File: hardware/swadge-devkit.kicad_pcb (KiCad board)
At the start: 2 copper layers, 100 x 100 mm, 60 parts, among them J1 USB_B_Micro, SW1 SW_SPDT, SW2 4-1437565-2, SW3 4-1437565-2, SW4 4-1437565-2, SW5 4-1437565-2, U1 ESP-12F, U2 MCP6001-OT, U3 MSA300, U4 AP1117-33, U5 BUS_PCIexpress, U6 DISP_OLED_UG-2864HSWEG01, U7 2460, U8 2460, U9 MMA8452Q

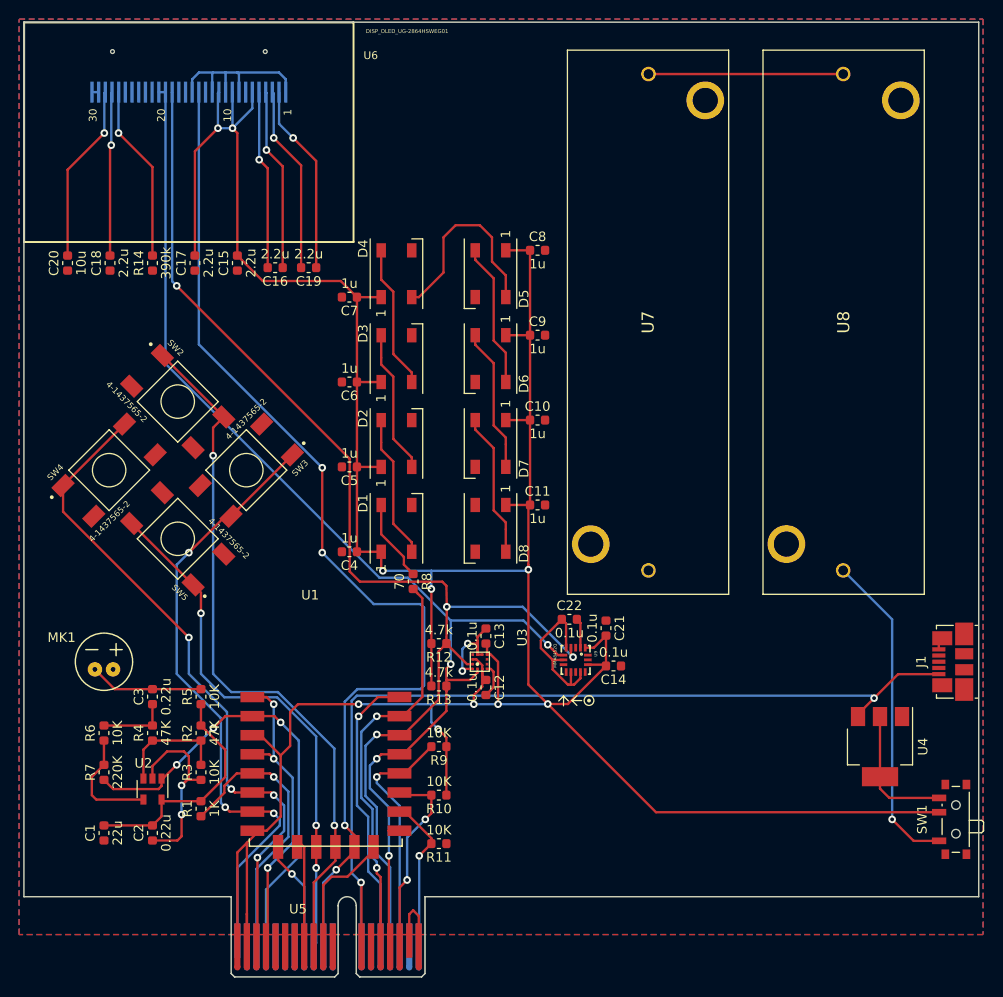
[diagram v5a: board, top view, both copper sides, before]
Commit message: Made board symmetrical wrt. the PCI connector
Moved batteries to the back, imported Swadge 2019 battery footprint
Reoriented accelerometers so they match orientation
Fattened up power traces
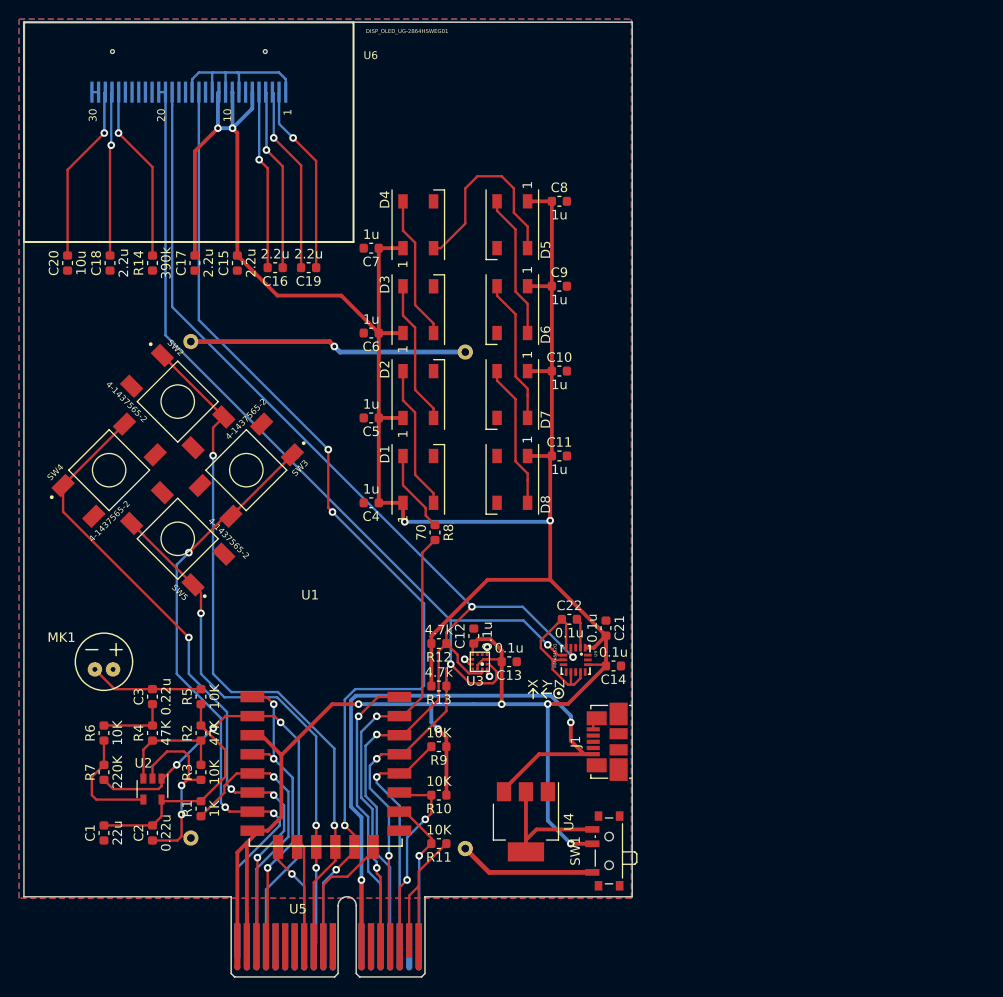
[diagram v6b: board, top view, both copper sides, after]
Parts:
- removed U7, U8: 2460, Swadge_Parts:2460
- added BT1: Battery, Swadge_Parts:BCAAPC, B.Cu at (131.0, 107.3)
- added BT2: Battery, Swadge_Parts:BCAAPC, B.Cu at (159.8, 107.3)
- moved U4 37.9 mm to (166.1, 131.1)
- moved J1 37.2 mm to (174.6, 122.7)
- moved SW1 36.5 mm to (174.5, 134.1)
- moved C10 5.62 mm to (169.6, 83.9)
- moved C11 5.62 mm to (169.6, 92.7)
- moved C4 5.62 mm to (149.9, 97.7)
- moved C5 5.62 mm to (149.9, 88.8)
- moved C6 5.62 mm to (149.9, 79.9)
- moved C7 5.62 mm to (149.9, 71.0)
- moved C8 5.62 mm to (169.6, 66.1)
- moved C9 5.62 mm to (169.6, 75.0)
- moved D1 5.62 mm to (154.8, 95.2)
- moved D2 5.62 mm to (154.8, 86.3)
- moved D3 5.62 mm to (154.8, 77.4)
- moved D4 5.62 mm to (154.8, 68.5)
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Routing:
- net Net-(BT1-Pad1): track 0.00 -> 29.2 mm, vias 0 -> 1
- net +5V: track 98.1 -> 73.8 mm
- net Net-(U7-Pad1): track 20.4 -> 0.00 mm
- net Net-(BT2-Pad1): track 34.1 -> 14.3 mm, vias 1 -> 0
- net +3V3: track 338.1 -> 319.4 mm, vias 10 -> 9
- net RX: track 42.8 -> 48.1 mm
- net SCL: track 132.8 -> 129.6 mm, vias 4 -> 3
- net MOSI: track 109.9 -> 107.2 mm
- net SDA: track 127.9 -> 130.2 mm
- net GND: track 80.0 -> 80.4 mm, vias 4 -> 5
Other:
- board size 100 x 100 mm -> 63.7 x 100 mm

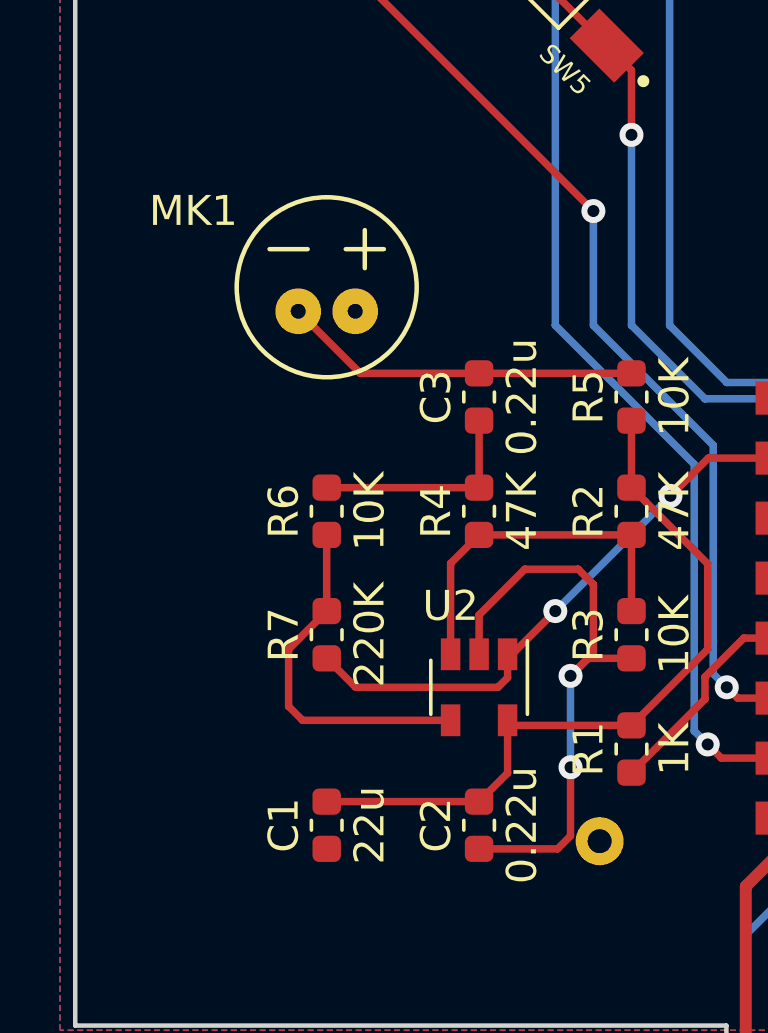
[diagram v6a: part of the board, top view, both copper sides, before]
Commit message: Moved mic away from battery
Updated DRC to use CNLohr's numbers
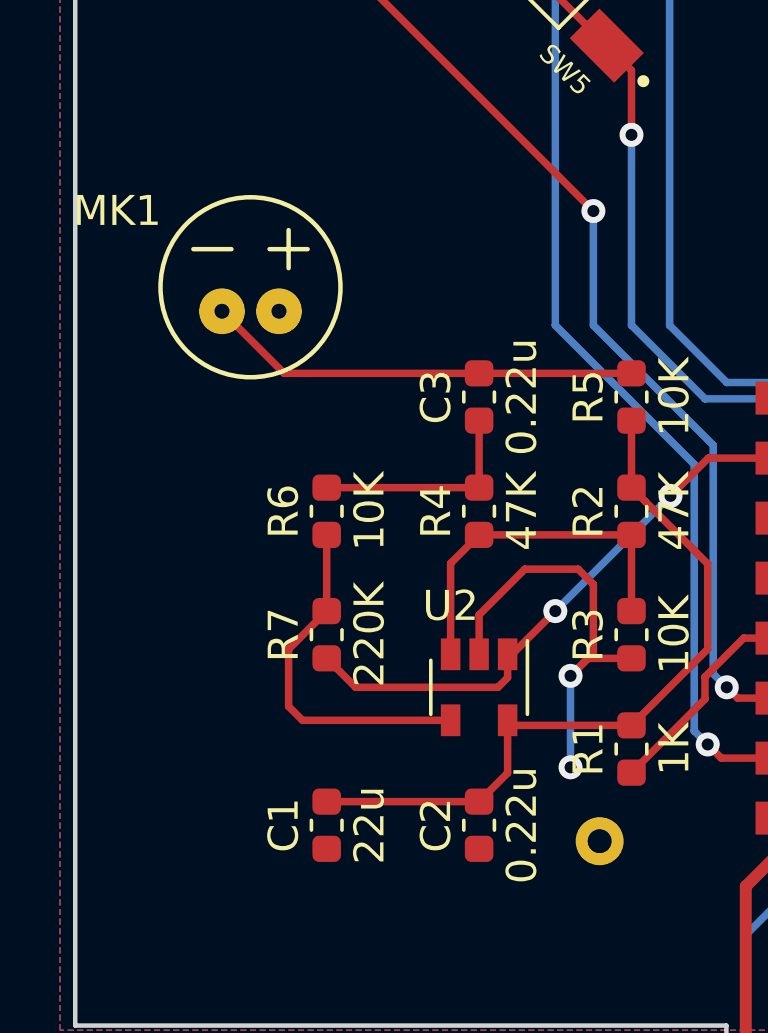
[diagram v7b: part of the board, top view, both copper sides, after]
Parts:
- moved MK1 2.54 mm to (119.4, 114.3)
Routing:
- net GND: track 80.4 -> 74.9 mm
- net Net-(C3-Pad2): track 12.0 -> 14.5 mm
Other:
- net class Default: clearance 0.2 -> 0.19558; trace_width 0.25 -> 0.3048; via_dia 0.8 -> 0.635; via_drill 0.4 -> 0.3556
- rule trace_clearance: 0.2 -> 0.19558
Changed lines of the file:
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@@
-(kicad_pcb (version 20171130) (host pcbnew "(5.0.0)")
+(kicad_pcb (version 20171130) (host pcbnew "(5.0.2)-1")
   (general
     (thickness 1.6)
     (drawings 25)
-    (tracks 579)
+    (tracks 576)
     (zones 0)
     (modules 60)
@@
   )
   (setup
-    (last_trace_width 0.4)
+    (last_trace_width 0.3048)
     (user_trace_width 0.4)
-    (trace_clearance 0.2)
+    (trace_clearance 0.19558)
     (zone_clearance 0.05)
     (zone_45_only no)
@@
     (segment_width 0.01)
     (edge_width 0.15)
-    (via_size 0.8)
-    (via_drill 0.4)
+    (via_size 0.635)
+    (via_drill 0.3556)
     (via_min_size 0.4)
     (via_min_drill 0.3)
@@
   (net 75 "Net-(BT2-Pad1)")
   (net_class Default "This is the default net class."
-    (clearance 0.2)
-    (trace_width 0.25)
-    (via_dia 0.8)
-    (via_drill 0.4)
+    (clearance 0.19558)
+    (trace_width 0.3048)
+    (via_dia 0.635)
+    (via_drill 0.3556)
     (uvia_dia 0.3)
     (uvia_drill 0.1)
@@
   )
   (module Swadge_Parts:POM-2738P-R (layer F.Cu)
-    (at 121.92 114.3 180)
+    (at 119.38 114.3 180)
     (fp_text reference MK1 (at 4.445 2.54 180) (layer F.SilkS)
       (effects (font (size 1 1) (thickness 0.15)))
@@
   (via (at 130.048 130.302) (size 0.8) (drill 0.4) (layers F.Cu B.Cu) (net 3))
   (segment (start 130.048 127.254) (end 130.048 130.302) (width 0.25) (layer B.Cu) (net 3))
-  (segment (start 130.048 130.302) (end 130.048 132.588) (width 0.25) (layer F.Cu) (net 3))
-  (segment (start 129.616 133.02) (end 127 133.02) (width 0.25) (layer F.Cu) (net 3))
-  (segment (start 130.048 132.588) (end 129.616 133.02) (width 0.25) (layer F.Cu) (net 3))
   (segment (start 127 126.535) (end 127 125.222) (width 0.25) (layer F.Cu) (net 3))
   (segment (start 127 125.222) (end 128.524 123.698) (width 0.25) (layer F.Cu) (net 3))
@@
   (segment (start 127 120.98) (end 121.92 120.98) (width 0.25) (layer F.Cu) (net 4))
   (segment (start 127 117.17) (end 132.08 117.17) (width 0.25) (layer F.Cu) (net 5))
-  (segment (start 123.04 117.17) (end 120.97 115.1) (width 0.25) (layer F.Cu) (net 5))
-  (segment (start 127 117.17) (end 123.04 117.17) (width 0.25) (layer F.Cu) (net 5))
+  (segment (start 120.5 117.17) (end 118.43 115.1) (width 0.25) (layer F.Cu) (net 5))
+  (segment (start 127 117.17) (end 120.5 117.17) (width 0.25) (layer F.Cu) (net 5))
   (segment (start 132.08 125.095) (end 132.08 122.555) (width 0.25) (layer F.Cu) (net 6))
   (segment (start 132.08 122.555) (end 127 122.555) (width 0.25) (layer F.Cu) (net 6))

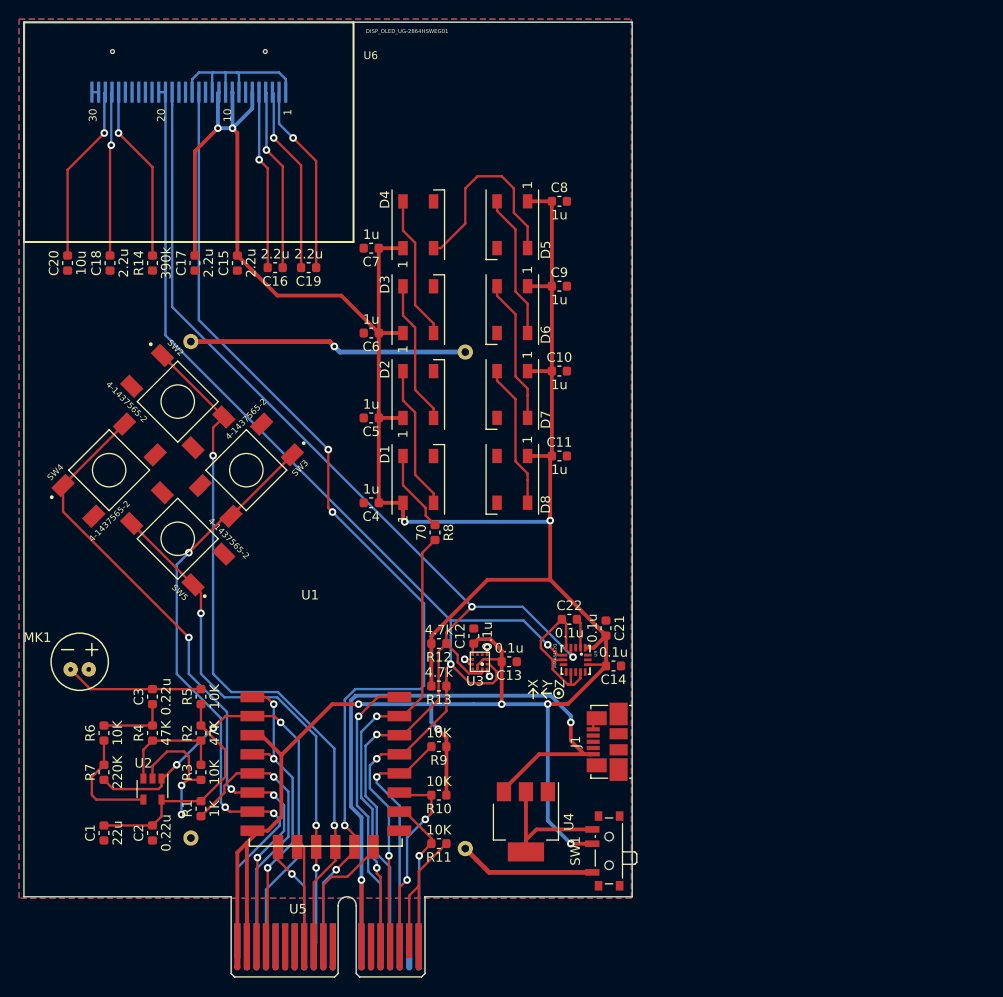
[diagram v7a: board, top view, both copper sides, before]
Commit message: Updated library with manufacturing info followiong cnlohr's kicad_for_mfg
Updated all traces (except accelerometer traces) to 0.0077in
Replaced microphone with bigger, cheaper one
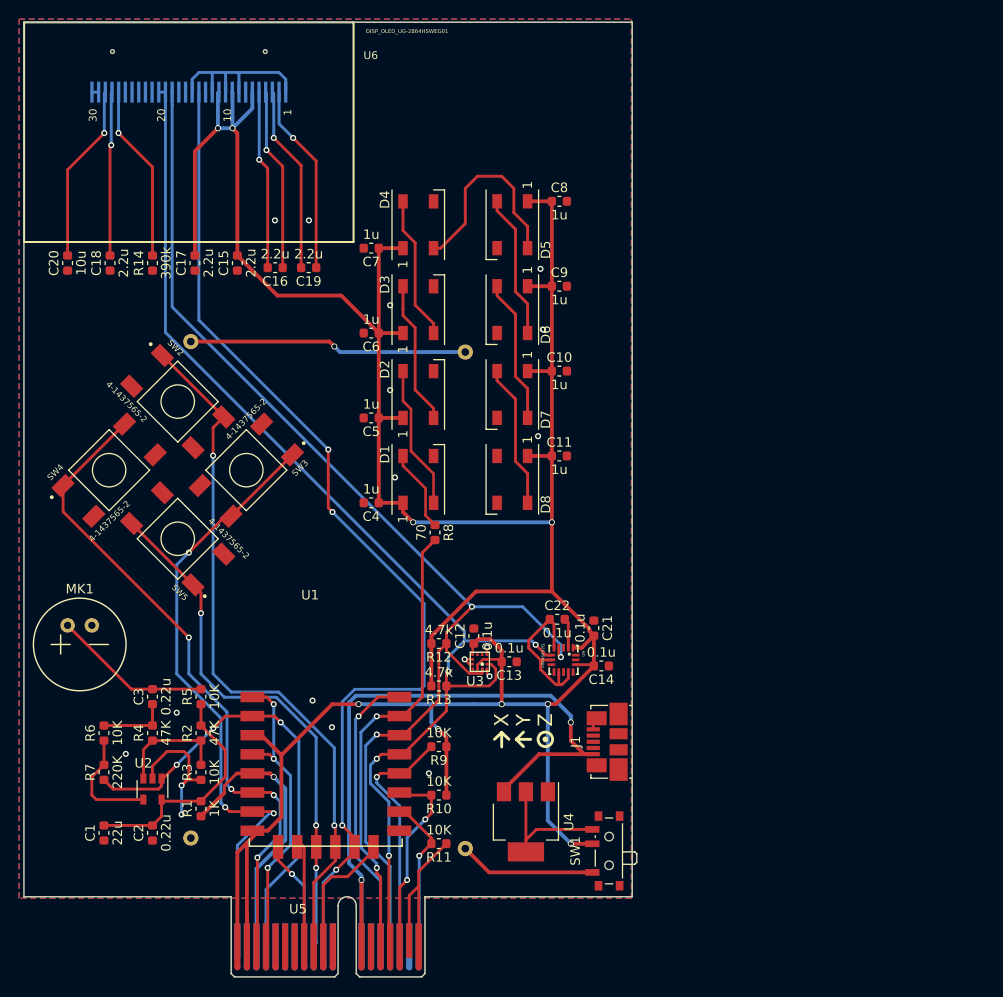
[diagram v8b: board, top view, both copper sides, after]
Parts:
- MK1: footprint Swadge_Parts:POM-2738P-R -> Swadge_Parts:CMA-4544PF-W
- moved MK1 1.81 mm to (119.4, 112.5)
- moved C14 1.27 mm to (174.0, 114.7)
- moved U9 1.27 mm to (170.1, 114.1)
- moved C21 1.27 mm to (173.2, 110.8)
- moved C22 1.27 mm to (169.4, 109.9)
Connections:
- D8 pad 2: Net-(D8-Pad2) -> (no net)
- J1 pad 2: Net-(J1-Pad2) -> (no net)
- J1 pad 3: Net-(J1-Pad3) -> (no net)
- J1 pad 4: Net-(J1-Pad4) -> (no net)
- U3 pad 10: Net-(U3-Pad10) -> (no net)
- U3 pad 5: Net-(U3-Pad5) -> (no net)
- U3 pad 6: Net-(U3-Pad6) -> (no net)
- U6 pad 13: Net-(U6-Pad13) -> (no net)
- U6 pad 16: Net-(U6-Pad16) -> (no net)
- U6 pad 17: Net-(U6-Pad17) -> (no net)
- U6 pad 21: Net-(U6-Pad21) -> (no net)
- U6 pad 22: Net-(U6-Pad22) -> (no net)
- U6 pad 23: Net-(U6-Pad23) -> (no net)
- U6 pad 24: Net-(U6-Pad24) -> (no net)
- U6 pad 25: Net-(U6-Pad25) -> (no net)
- U6 pad 7: Net-(U6-Pad7) -> (no net)
- U9 pad 11: Net-(U9-Pad11) -> (no net)
- U9 pad 9: Net-(U9-Pad9) -> (no net)
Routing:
- net SDA: track 130.2 -> 126.9 mm
- net +3V3: track 319.4 -> 316.8 mm
- net Net-(C3-Pad2): track 14.5 -> 16.7 mm
- net SCL: track 129.6 -> 129.1 mm
- net GND: vias 5 -> 16
- net (no net): vias 0 -> 2
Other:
- net class Power added: clearance 0.19558, trace_width 0.4, via_dia 0.635, via_drill 0.45
- net class Thin added: clearance 0.19558, trace_width 0.25, via_dia 0.635, via_drill 0.3556
- board text added: "X"
- board text added: "Y"
- board text added: "Z"
